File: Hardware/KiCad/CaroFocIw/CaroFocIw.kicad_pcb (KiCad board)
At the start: 4 copper layers, 140 x 70 mm, 97 parts, among them J1 Conn_01x02, J10 Conn_01x05, J11 Conn_01x05, J12 Conn_01x02, J13 Conn_01x02, J14 Conn_01x03, J15 Conn_01x03, J16 Conn_01x03, J17 Conn_01x05, J18 Conn_01x05, J19 Conn_01x02, J2 Conn_01x01, J3 Conn_01x01, J4 Conn_01x01, J5 Conn_01x01, J6 Conn_01x02, J7 Conn_01x03, J8 Conn_01x03, J9 Conn_01x03, Q1 Q_NMOS_SGD, Q2 Q_NMOS_SGD, Q3 Q_NMOS_SGD, Q4 Q_NMOS_SGD, Q5 Q_NMOS_SGD, Q6 Q_NMOS_SGD, U1 TCAN332, U2 STM32F405RGTx, U3 TLE7185-1E, U4 ACS711xEXLT-15AB, U5 AS5048A, U6 ACS711xEXLT-15AB, U7 ACS711xEXLT-15AB, U8 LMR16006YQ3

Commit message: Some more layout work
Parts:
- added J20: Conn_01x06, Connector_PinHeader_2.00mm:PinHeader_1x06_P2.00mm_Vertical, F.Cu at (208.0, 158.0)
- added J21: Conn_01x06, Connector_PinHeader_2.00mm:PinHeader_1x06_P2.00mm_Vertical, F.Cu at (212.0, 158.0)
- added J22: Conn_01x02, Connector_PinHeader_2.00mm:PinHeader_1x02_P2.00mm_Vertical, F.Cu at (199.0, 138.0)
- added J23: Conn_01x03, Connector_PinHeader_2.00mm:PinHeader_1x03_P2.00mm_Vertical, F.Cu at (178.0, 123.0)
- added J24: Conn_01x03, Connector_PinHeader_2.00mm:PinHeader_1x03_P2.00mm_Vertical, F.Cu at (212.0, 93.0)
- added J25: Conn_01x03, Connector_PinHeader_2.00mm:PinHeader_1x03_P2.00mm_Vertical, F.Cu at (242.0, 127.0)
- C1, C10, C11, C12, C13, C14, C2, C21, C22, C23, C3, C36, C37, C38, C39, C4, C40, C41, C5, C6, C7, C8, C9: footprint Capacitors_SMD:C_0603 -> Capacitor_SMD:C_0603_1608Metric
- J10, J11: value Conn_01x05 -> Conn_01x06; footprint Pin_Headers:Pin_Header_Straight_1x05_Pitch2.00mm -> Connector_PinHeader_2.00mm:PinHeader_1x06_P2.00mm_Vertical
- J12, J6: footprint Pin_Headers:Pin_Header_Straight_1x02_Pitch2.00mm -> Connector_PinHeader_2.00mm:PinHeader_1x02_P2.00mm_Vertical
- J13, J19: value Conn_01x02 -> Conn_01x03; footprint Pin_Headers:Pin_Header_Straight_1x02_Pitch2.00mm -> Connector_PinHeader_2.00mm:PinHeader_1x03_P2.00mm_Vertical
- J14, J15, J7, J8, J9: footprint Pin_Headers:Pin_Header_Straight_1x03_Pitch2.00mm -> Connector_PinHeader_2.00mm:PinHeader_1x03_P2.00mm_Vertical
- J16: value Conn_01x03 -> Conn_01x02; footprint Pin_Headers:Pin_Header_Straight_1x03_Pitch2.00mm -> Connector_PinHeader_2.00mm:PinHeader_1x02_P2.00mm_Vertical
- J17, J18: value Conn_01x05 -> Conn_01x03; footprint Pin_Headers:Pin_Header_Straight_1x05_Pitch2.00mm -> Connector_PinHeader_2.00mm:PinHeader_1x03_P2.00mm_Vertical
- moved J13 83.7 mm to (108.0, 123.0), turned to 0 degrees
- moved J14 56.9 mm to (142.0, 93.0), turned to 270 degrees
- moved J15 50.3 mm to (172.0, 127.0), turned to 180 degrees
- moved J18 49.5 mm to (219.0, 109.0), turned to 135 degrees
- moved J17 44.3 mm to (194.0, 116.0), turned to 225 degrees
- moved J16 36.5 mm to (190.0, 140.0), turned to 135 degrees
- moved J19 27.3 mm to (226.0, 134.0), turned to 45 degrees
- moved R1 7.57 mm to (153.0, 140.5), turned to 180 degrees
- moved C22 2.24 mm to (141.0, 129.0)
- moved C23 2.24 mm to (141.0, 127.0)
- moved U1 1.00 mm to (153.0, 143.0)
- moved C1 0.50 mm to (150.0, 143.5)
- moved C6 0.50 mm to (149.0, 140.5)
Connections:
- J13 pad 1: GNDPWR -> GNDPWR_A
- J13 pad 2: +BATT -> GNDPWR_A
- J14 pad 1: AGND_U -> GNDPWR_A
- J14 pad 2: /CurrentSensingU/AnalogOut -> GNDPWR_A
- J14 pad 3: 3.3VA_U -> GNDPWR_A
- J15 pad 1: AGND_V -> GNDPWR_A
- J15 pad 2: /CurrentSensingV/AnalogOut -> GNDPWR_A
- J15 pad 3: 3.3VA_V -> GNDPWR_A
- J16 pad 1: AGND_W -> GNDPWR
- J16 pad 2: /CurrentsensingW/AnalogOut -> +BATT
- J17 pad 1: /GateDriver/~LogicUH -> AGND_U
- J17 pad 2: GND_B -> /CurrentSensingU/AnalogOut
- J17 pad 3: /GateDriver/LogicGdEna -> 3.3VA_U
- J18 pad 1: /GateDriver/LogicUL -> AGND_V
- J18 pad 2: /GateDriver/~LogicVH -> /CurrentSensingV/AnalogOut
- J18 pad 3: /GateDriver/LogicVL -> 3.3VA_V
- J19 pad 1: /PcbToPcbConnector/CanHB -> AGND_W
- J19 pad 2: /PcbToPcbConnector/CanLB -> /CurrentsensingW/AnalogOut
- U2 pad 55: /MCU/~GateDriverErr1 -> /MCU/GateDriverEnable
- U2 pad 56: /MCU/~GateDriverErr2 -> /MCU/~GateDriverErr1
- U2 pad 57: /MCU/GateDriverEnable -> /MCU/~GateDriverErr2
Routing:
- net /HalfBridgeV/GateL: track 0.00 -> 43.6 mm, vias 0 -> 2
- net /MCU/CurrentV: track 0.00 -> 41.4 mm
- net /MCU/CurrentU: track 0.00 -> 39.1 mm, vias 0 -> 2
- net +BATT: track 1.00 -> 38.2 mm, vias 0 -> 45
- net /HalfBridgeV/GateH: track 0.00 -> 33.0 mm, vias 0 -> 2
- net /HalfBridgeU/GateL: track 0.00 -> 28.1 mm, vias 0 -> 2
- net +3V3: track 10.7 -> 38.1 mm, vias 0 -> 8
- net /MCU/~GateDriverErr2: track 0.00 -> 25.9 mm, vias 0 -> 1
- net /MCU/CurrentW: track 0.00 -> 24.8 mm, vias 0 -> 1
- net /MCU/~GateDriverErr1: track 0.00 -> 24.4 mm, vias 0 -> 1
- net /HalfBridgeW/GateL: track 0.00 -> 21.2 mm, vias 0 -> 2
- net /MCU/GateDriverEnable: track 0.00 -> 20.0 mm, vias 0 -> 1
- net /HalfBridgeU/GateH: track 0.00 -> 17.1 mm, vias 0 -> 2
- net /HalfBridgeW/GateH: track 0.00 -> 14.2 mm, vias 0 -> 2
- net /MCU/LogicWL: track 0.00 -> 11.9 mm, vias 0 -> 1
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- added copper zone on In2.Cu, net +3V3
- added copper zone on In2.Cu, net +BATT
- added copper zone on In1.Cu, net /CurrentSensingU/PhaseIn
- added copper zone on In1.Cu, net /CurrentSensingV/PhaseOut
- added copper zone on In1.Cu, net /CurrentsensingW/PhaseIn
- added copper zone on F.Cu, net BattA
- added copper zone on B.Cu, net GND
- added copper zone on In1.Cu, net GNDPWR
- added copper zone on In2.Cu, net GNDPWR
- added copper zone on In1.Cu, net GND_B
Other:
- outline, holes or cut-outs redrawn

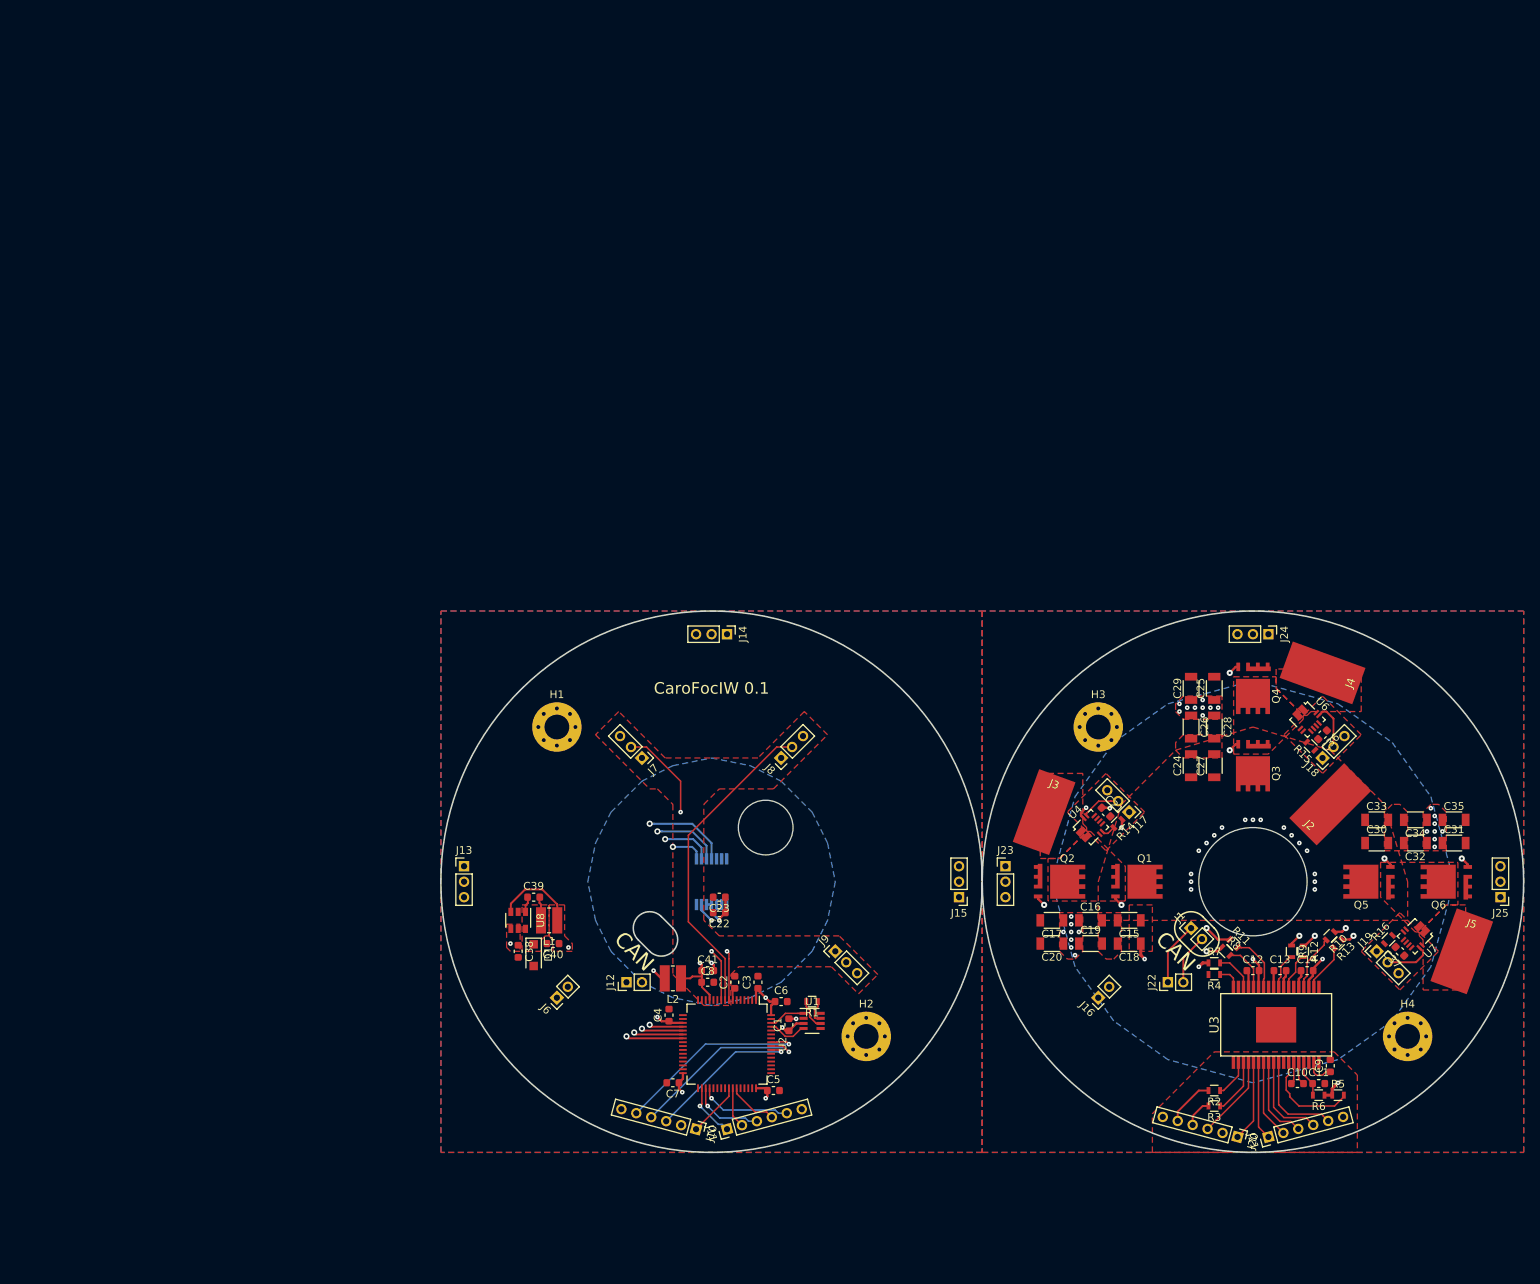
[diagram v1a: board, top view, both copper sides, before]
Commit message: Added DcLinkVoltageSensing, fixad a bug in schematic, routed remaining nets, got rid of all ERC and DRC errors and changed some mechanical aspects
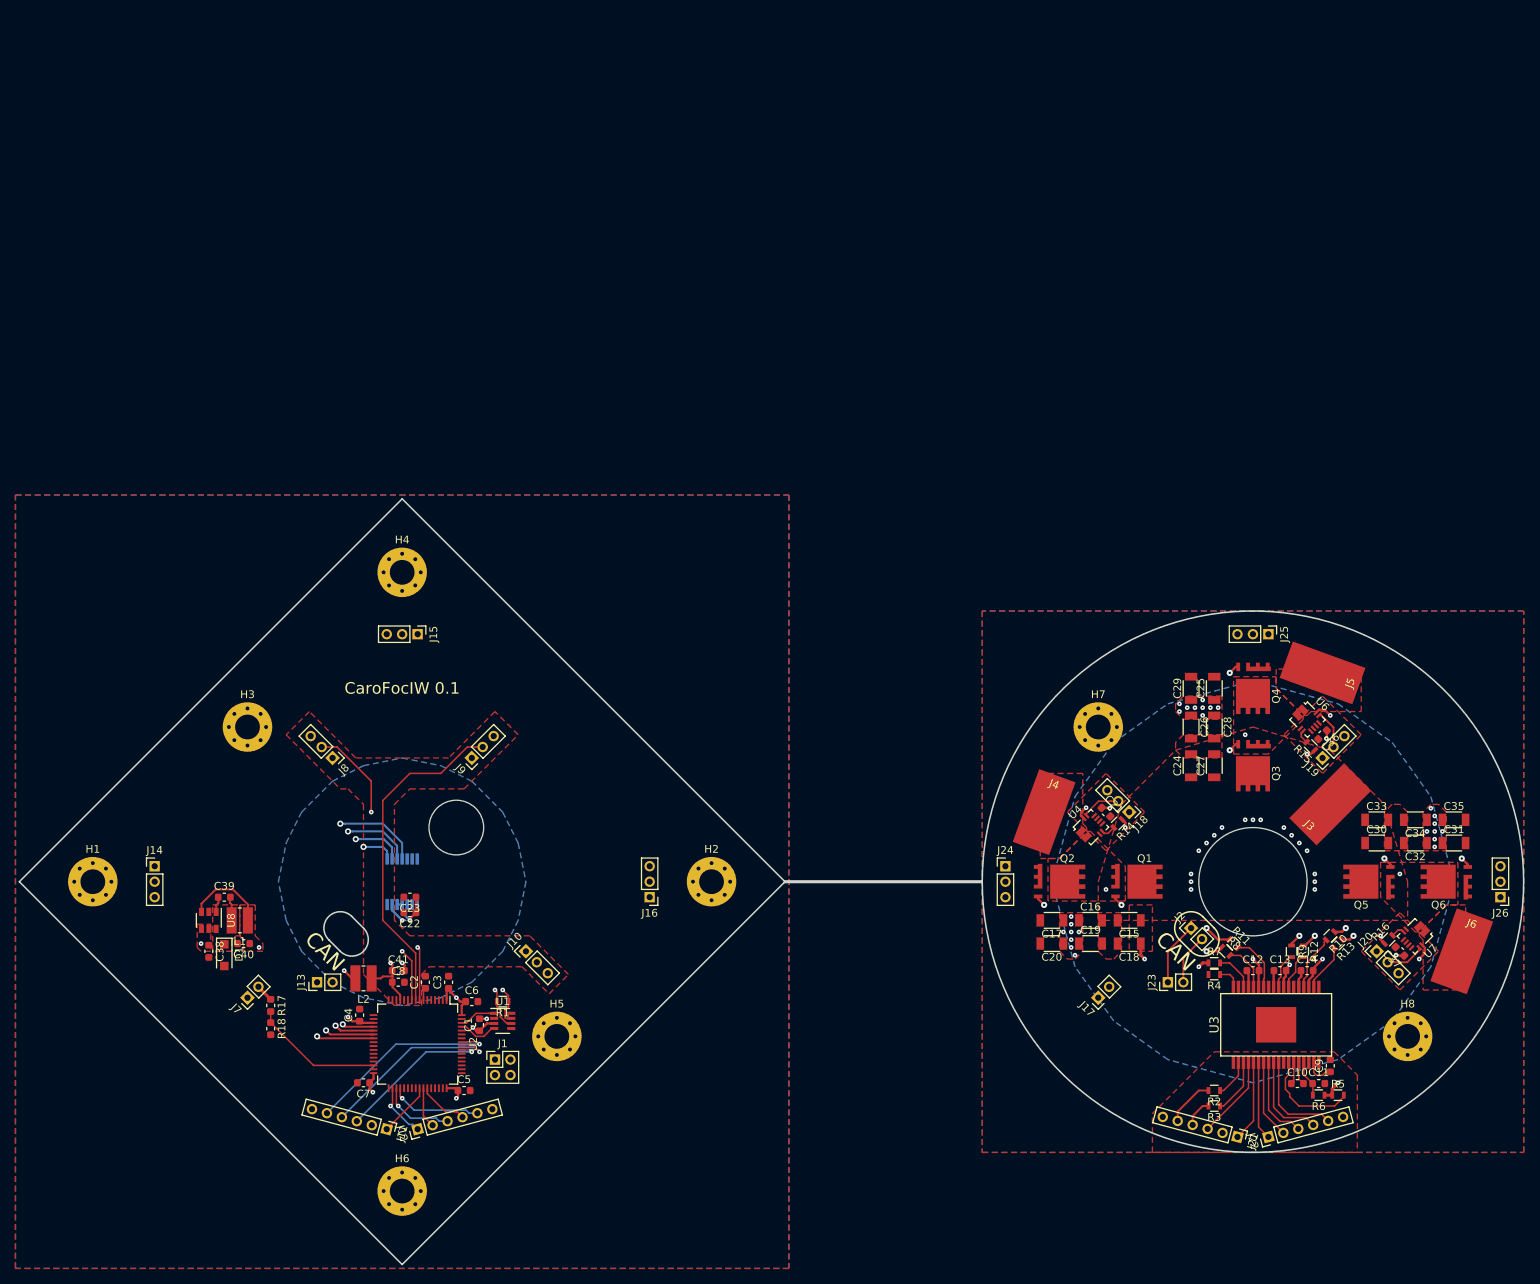
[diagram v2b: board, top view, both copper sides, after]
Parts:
- added H1: MountingHole_Pad, MountingHole:MountingHole_3.2mm_M3_Pad_Via, F.Cu at (60.0, 125.0)
- added H2: MountingHole_Pad, MountingHole:MountingHole_3.2mm_M3_Pad_Via, F.Cu at (140.0, 125.0)
- added H4: MountingHole_Pad, MountingHole:MountingHole_3.2mm_M3_Pad_Via, F.Cu at (100.0, 85.0)
- added H6: MountingHole_Pad, MountingHole:MountingHole_3.2mm_M3_Pad_Via, F.Cu at (100.0, 165.0)
- added J1: Conn_01x04, Connector_PinHeader_2.00mm:PinHeader_2x02_P2.00mm_Vertical, F.Cu at (112.0, 148.0)
- added R17: 47k, Resistor_SMD:R_0603_1608Metric, F.Cu at (83.0, 141.0)
- added R18: 10k, Resistor_SMD:R_0603_1608Metric, F.Cu at (83.0, 144.0)
- moved C1 40.0 mm to (110.0, 143.5)
- moved C2 40.0 mm to (103.0, 138.0)
- moved C22 40.0 mm to (101.0, 129.0)
- moved C23 40.0 mm to (101.0, 127.0)
- moved C3 40.0 mm to (106.0, 138.0)
- moved C38 40.0 mm to (75.0, 134.0)
- moved C39 40.0 mm to (77.0, 127.0)
- moved C4 40.0 mm to (94.5, 142.2)
- moved C40 40.0 mm to (79.5, 133.0)
- moved C41 40.0 mm to (99.5, 136.5)
- moved C5 40.0 mm to (108.0, 152.0)
- moved C6 40.0 mm to (109.0, 140.5)
- moved C7 40.0 mm to (95.0, 151.0)
- moved C8 40.0 mm to (99.5, 138.0)
- moved D1 40.0 mm to (77.0, 134.5)
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- renumbered H1 to H3, H2 to H5, H3 to H7, H4 to H8, J9 to J10, J10 to J11, J11 to J12, J12 to J13, J13 to J14, J14 to J15, J15 to J16, J16 to J17, J17 to J18, J18 to J19, J1 to J2, J19 to J20, J20 to J21, J21 to J22, J22 to J23, J23 to J24, J24 to J25, J25 to J26, J2 to J3, J3 to J4, J4 to J5, J5 to J6, J6 to J7, J7 to J8, J8 to J9
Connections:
- net Net-(C2-Pad1) renamed /MCU/~RST
- U2 pad 30: Net-(U2-Pad30) -> /DcLinkVoltageSensing/AnalogOut
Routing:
- net /Can/CanH: track 3.10 -> 32.7 mm, vias 0 -> 1
- net /Can/CanL: track 3.93 -> 29.4 mm, vias 0 -> 1
- net /DcLinkVoltageSensing/AnalogOut: track 0.00 -> 17.0 mm
- net 3.3VA_V: track 0.00 -> 4.56 mm, vias 0 -> 3
- net 3.3VA_W: track 0.00 -> 4.56 mm, vias 0 -> 3
- net BattA: track 9.73 -> 12.0 mm
- net /MCU/CurrentV: track 41.4 -> 43.3 mm
- net Net-(R15-Pad2): track 0.00 -> 1.78 mm
- net Net-(R16-Pad2): track 0.00 -> 1.78 mm
- net /CurrentSensingV/AnalogOut: track 6.13 -> 5.05 mm
- net /CurrentsensingW/AnalogOut: track 6.13 -> 5.05 mm
- net /CurrentSensingV/PhaseIn: track 2.25 -> 3.19 mm, vias 0 -> 2
- net /CurrentsensingW/PhaseIn: vias 1 -> 2
- net /CurrentSensingU/PhaseIn: vias 1 -> 2
- added copper zone on In1.Cu, net /CurrentSensingV/PhaseIn
- removed copper zone on In1.Cu, net /CurrentSensingV/PhaseOut
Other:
- board size 140 x 70 mm -> 194.5 x 99 mm

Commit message: Bugfix: placement of one board-to-board connector for current sensing phase U was not aligned with other board. Lots of layout refinements including lower inductance gate switching path, better ground planes and concept for mounting ball heads later on. SWD connector must still be placed elsewhere
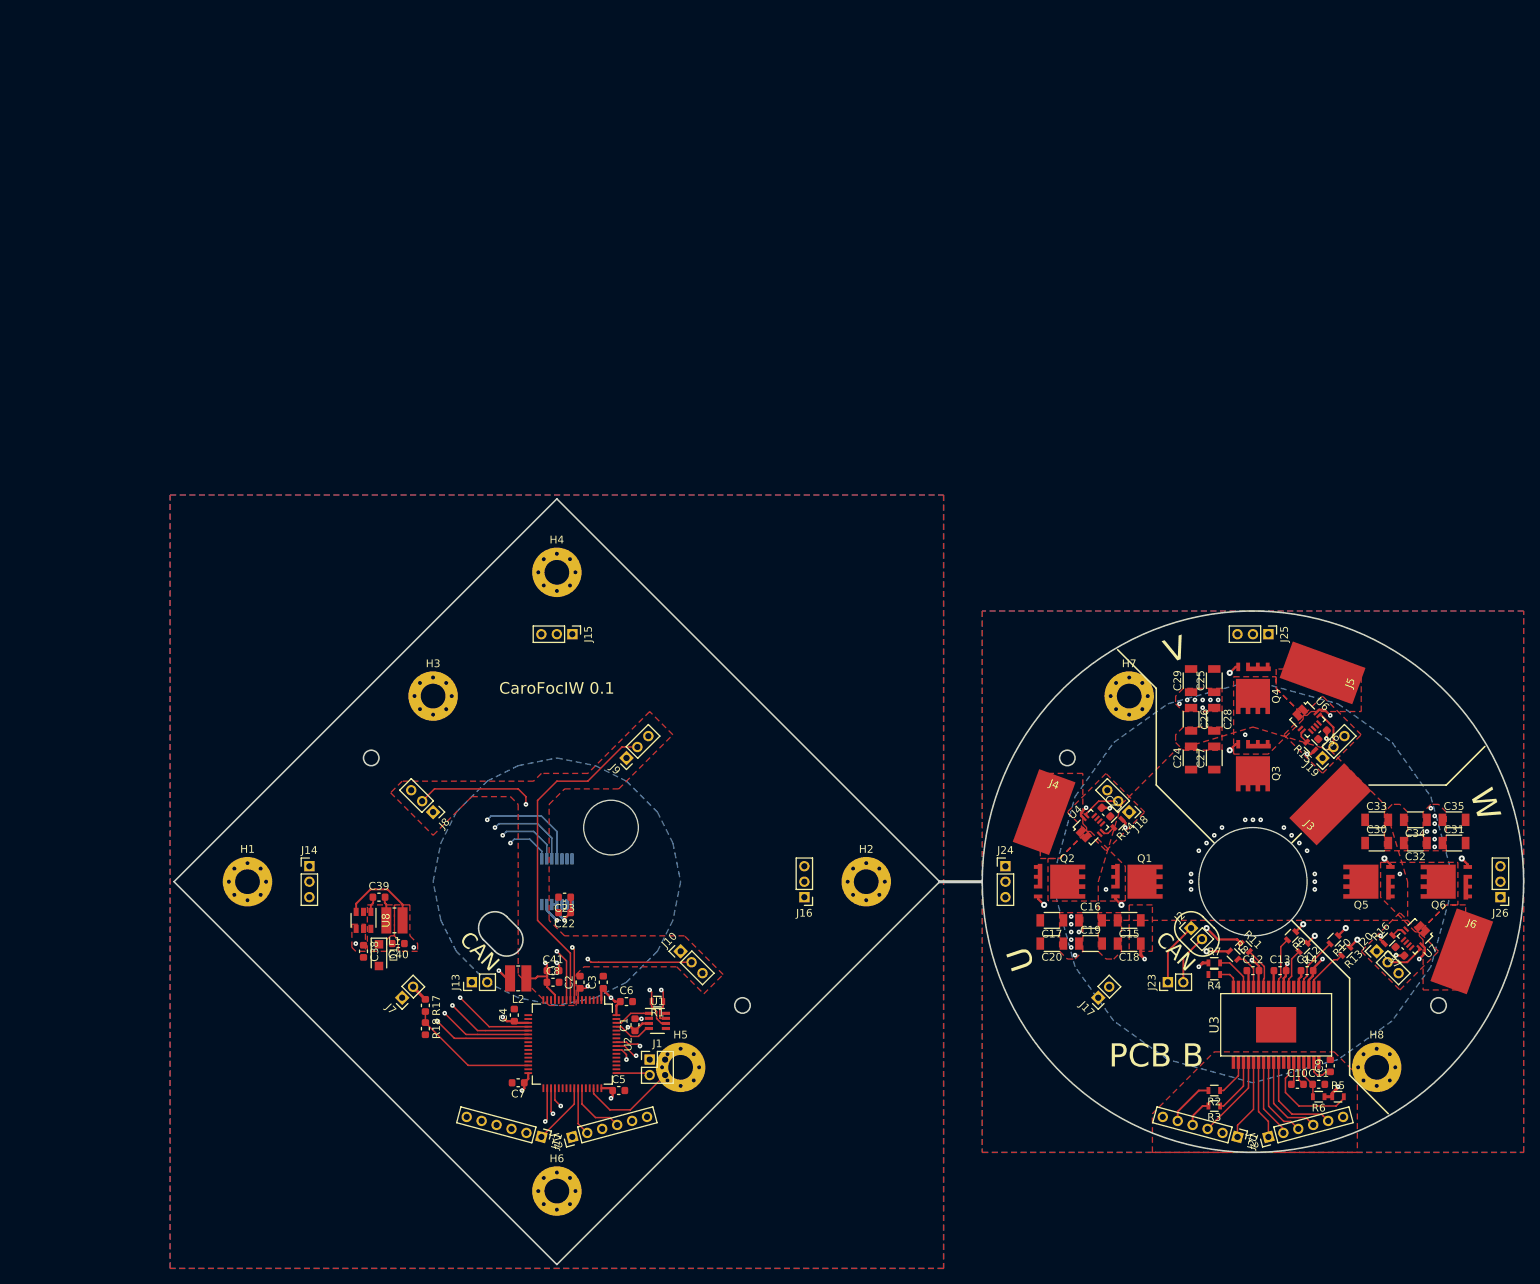
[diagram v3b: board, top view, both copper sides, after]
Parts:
- moved H3 24.3 mm to (104.0, 101.0)
- moved C1 20.1 mm to (130.1, 143.5)
- moved J11 20.0 mm to (118.0, 158.0)
- moved J12 20.0 mm to (122.0, 158.0)
- moved C2 20.0 mm to (123.0, 138.0)
- moved C22 20.0 mm to (121.0, 129.0)
- moved C23 20.0 mm to (121.0, 127.0)
- moved C3 20.0 mm to (126.0, 138.0)
- moved C38 20.0 mm to (95.0, 134.0)
- moved C39 20.0 mm to (97.0, 127.0)
- moved C4 20.0 mm to (114.5, 142.2)
- moved C40 20.0 mm to (99.5, 133.0)
- moved C41 20.0 mm to (119.5, 136.5)
- moved C5 20.0 mm to (128.0, 152.0)
- moved C6 20.0 mm to (129.0, 140.5)
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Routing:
- net +BATT: track 38.2 -> 10.5 mm, vias 45 -> 41
- net /MCU/~RST: track 1.62 -> 25.6 mm, vias 0 -> 1
- net /MCU/SWDIO: track 0.00 -> 12.7 mm
- net /Encoder/EncoderMosi: track 50.0 -> 55.4 mm
- net /Encoder/EncoderMiso: track 45.0 -> 50.1 mm
- net /Encoder/EncoderSclk: track 40.1 -> 44.7 mm
- net /MCU/CurrentU: track 39.1 -> 43.7 mm
- net /MCU/SWCLK: track 0.00 -> 4.40 mm
- net /HalfBridgeU/GateL: track 28.1 -> 32.3 mm
- net /Encoder/~EncoderCs: track 35.5 -> 39.4 mm
- net /MCU/~GateDriverErr2: track 25.9 -> 28.8 mm
- net /GateDriver/Gate_U_L_bR: track 7.45 -> 5.45 mm
- net /HalfBridgeV/GateH: track 33.0 -> 31.0 mm
- net /GateDriver/GateVHbR: track 4.70 -> 6.58 mm
- net /MCU/LogicUL: track 7.15 -> 8.73 mm
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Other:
- board size 194.5 x 99 mm -> 174.5 x 99 mm
- board text added: "PCB B"
- board text added: "U"
- board text added: "V"
- board text added: "W"
